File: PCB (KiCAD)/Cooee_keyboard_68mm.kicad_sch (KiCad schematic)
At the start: 99 parts, among them J1 Conn_01x15_Pin

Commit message: finished routing new smaller keyboard
finished routing new smaller keyboard
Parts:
- removed H1: MountingHole, MountingHole:MountingHole_3.2mm_M3_ISO7380_Pad, symbol Mechanical:MountingHole
- H4, H5: footprint MountingHole:MountingHole_3.2mm_M3_ISO7380_Pad -> MountingHole:MountingHole_3.2mm_M3
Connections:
- net COL1: now also D5.1 (K); no longer D7.1 (K)
- net COL2: now also D51.1 (K), D7.1 (K); no longer D14.1 (K), D5.1 (K)
- net COL3: now also D14.1 (K); no longer D17.1 (K)
- net COL4: now also D17.1 (K); no longer D21.1 (K)
- net COL5: now also D21.1 (K); no longer D22.1 (K), D92.1 (K)
- net COL6: now also D22.1 (K), D92.1 (K); no longer D27.1 (K), D93.1 (K)
- net COL7: now also D27.1 (K), D93.1 (K), J1.4 (Pin_4); no longer D28.2 (A), D31.1 (K), J1.9 (Pin_9)
- net COL8: now also D28.2 (A), D31.1 (K), J1.3 (Pin_3); no longer D51.1 (K), D52.1 (K), D54.1 (K), J1.8 (Pin_8)
- net COL9: now also D52.1 (K), J1.2 (Pin_2); no longer D39.1 (K), D44.1 (K), J1.7 (Pin_7)
- net ROW1: now also J1.9 (Pin_9), SWe29.1; no longer J1.6 (Pin_6)
- net ROW2: now also J1.8 (Pin_8), SWe36.1, SWe37.1; no longer J1.5 (Pin_5), SWe29.1
- net ROW3: now also J1.7 (Pin_7), SWe39.1; no longer J1.4 (Pin_4), SWe36.1
- net ROW4: now also J1.6 (Pin_6), SWe17.1, SWe24.1; no longer J1.3 (Pin_3), SWe39.1, SWe47.1
- net ROW5: now also J1.5 (Pin_5), SWe2.1, SWe47.1, SWe50.1; no longer J1.2 (Pin_2), SWe17.1, SWe24.1
- removed net ROW6: J1.1 (Pin_1), SWe2.1, SWe37.1, SWe50.1
- new net COL10: D39.1 (K), D44.1 (K), D54.1 (K), J1.1 (Pin_1)
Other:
- moved on the sheet: D14, D17, D21, D22, D27, D28, D3, D31, D32, D39, D43, D44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

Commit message: finished keyboard at 67mm
started work on esp32 motherboard
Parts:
- removed H4, H5, H7: MountingHole, MountingHole:MountingHole_3.2mm_M3, symbol Mechanical:MountingHole
- removed J1: Conn_01x15_Pin, Connector_PinHeader_2.54mm:PinHeader_1x15_P2.54mm_Vertical, symbol Connector:Conn_01x15_Pin
- added D4, D40, D47, D6: SS24, Diode_SMD:D_0805_2012Metric, symbol Diode:SS24
- added J1: Conn_02x20_Counter_Clockwise, Connector_PinHeader_2.54mm:PinHeader_2x20_P2.54mm_Vertical_SMD, symbol Connector_Generic:Conn_02x20_Counter_Clockwise
- added J2, J3, J4, J5, J6, J7: Conn_01x01_Pin, USB4105-GF-A (1):Lil_Pad, symbol Connector:Conn_01x01_Pin
- added R2, R3, R4, R6: R, Resistor_SMD:R_0805_2012Metric_Pad1.20x1.40mm_HandSolder, symbol Device:R
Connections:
- net COL1: now also J1.1 (Pin_1), J1.2 (Pin_2)
- net COL10: now also J1.39 (Pin_39), J1.40 (Pin_40)
- net COL2: now also J1.5 (Pin_5), J1.6 (Pin_6)
- net COL3: now also J1.10 (Pin_10), J1.9 (Pin_9)
- net COL4: now also J1.15 (Pin_15), J1.16 (Pin_16)
- net COL5: now also J1.19 (Pin_19), J1.20 (Pin_20)
- net COL6: now also J1.27 (Pin_27), J1.28 (Pin_28)
- net COL7: now also J1.33 (Pin_33), J1.34 (Pin_34)
- net COL8: now also J1.35 (Pin_35), J1.36 (Pin_36)
- net COL9: now also J1.37 (Pin_37), J1.38 (Pin_38)
- net ROW1: now also J1.3 (Pin_3), J1.4 (Pin_4)
- net ROW2: now also J1.7 (Pin_7), J1.8 (Pin_8)
- net ROW3: now also J1.11 (Pin_11), J1.12 (Pin_12)
- net ROW4: now also J1.13 (Pin_13), J1.14 (Pin_14)
- net ROW5: now also J1.17 (Pin_17), J1.18 (Pin_18)
- new net: D4.1 (K), R2.1
- new net: D40.1 (K), R4.1
- new net: D6.1 (K), R3.1
- new net: D47.1 (K), R6.1
- new net +3.3V: D4.2 (A), D40.2 (A), D47.2 (A), D6.2 (A), J1.31 (Pin_31), J1.32 (Pin_32)
- new net GND: J1.29 (Pin_29), J1.30 (Pin_30), R2.2, R3.2, R4.2, R6.2
- new net SPARE1: J1.26 (Pin_26), J2.1 (Pin_1)
- new net SPARE2: J1.25 (Pin_25), J3.1 (Pin_1)
- new net SPARE3: J1.24 (Pin_24), J4.1 (Pin_1)
- new net SPARE4: J1.23 (Pin_23), J5.1 (Pin_1)
- new net SPARE5: J1.22 (Pin_22), J6.1 (Pin_1)
- new net SPARE6: J1.21 (Pin_21), J7.1 (Pin_1)
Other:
- moved on the sheet: D10, D11, D12, D13, D14, D15, D16, D17, D18, D19, D2, D20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

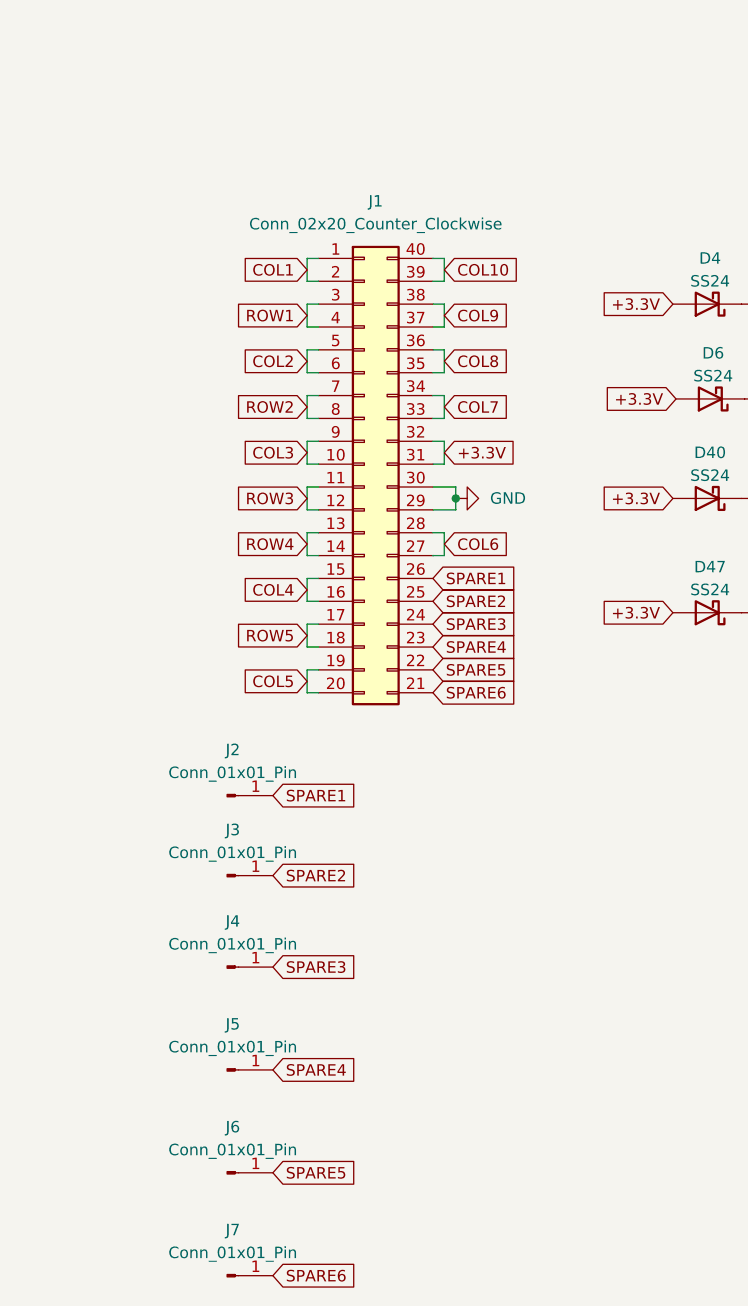
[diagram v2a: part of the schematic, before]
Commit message: more PCB work
should have the 90 degree SMD header pins lined up to mount now, unfortunately I've invalidated the keyboard prototypes I already bought
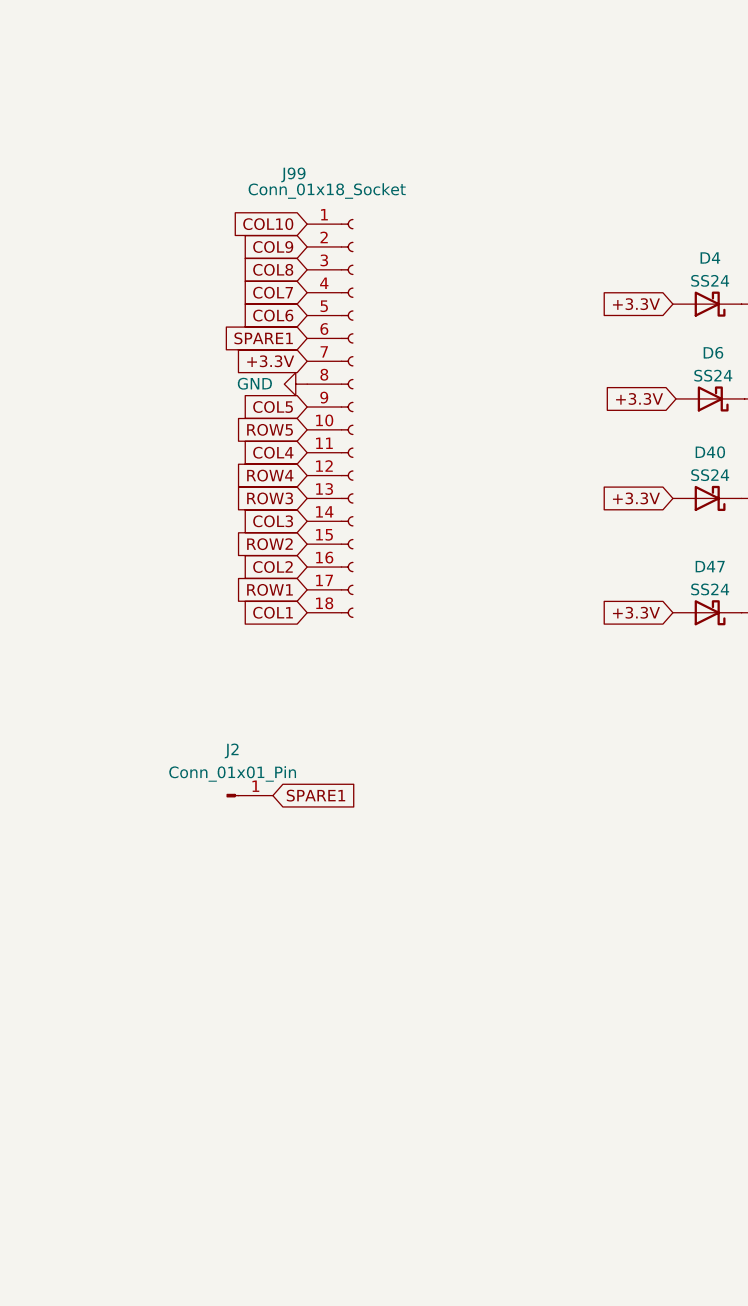
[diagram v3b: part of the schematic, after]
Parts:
- removed J1: Conn_02x20_Counter_Clockwise, Connector_PinHeader_2.54mm:PinHeader_2x20_P2.54mm_Vertical_SMD, symbol Connector_Generic:Conn_02x20_Counter_Clockwise
- removed J3, J4, J5, J6, J7: Conn_01x01_Pin, USB4105-GF-A (1):Lil_Pad, symbol Connector:Conn_01x01_Pin
- added J99: Conn_01x18_Socket, USB4105-GF-A (1):SMD_Header_1x18_P2.54mm, symbol Connector:Conn_01x18_Socket
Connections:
- net +3.3V: now also J99.7 (Pin_7)
- net COL1: now also J99.18 (Pin_18)
- net COL10: now also J99.1 (Pin_1)
- net COL2: now also J99.16 (Pin_16)
- net COL3: now also J99.14 (Pin_14)
- net COL4: now also J99.11 (Pin_11)
- net COL5: now also J99.9 (Pin_9)
- net COL6: now also J99.5 (Pin_5)
- net COL7: now also J99.4 (Pin_4)
- net COL8: now also J99.3 (Pin_3)
- net COL9: now also J99.2 (Pin_2)
- net GND: now also J99.8 (Pin_8)
- net ROW1: now also J99.17 (Pin_17)
- net ROW2: now also J99.15 (Pin_15)
- net ROW3: now also J99.13 (Pin_13)
- net ROW4: now also J99.12 (Pin_12)
- net ROW5: now also J99.10 (Pin_10)
- net SPARE1: now also J99.6 (Pin_6)

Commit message: new IC choices for GPS, audio and power
also added a keyboard IC to the keyboard to preventing wasting precious ESP32 GPIOs
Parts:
- removed J2: Conn_01x01_Pin, USB4105-GF-A (1):Lil_Pad, symbol Connector:Conn_01x01_Pin
- removed J99: Conn_01x18_Socket, USB4105-GF-A (1):SMD_Header_1x18_P2.54mm, symbol Connector:Conn_01x18_Socket
- added R1, R5, R7: 10k, Resistor_SMD:R_0805_2012Metric_Pad1.20x1.40mm_HandSolder, symbol Device:R
- added U1: TCA8418RTWR, USB4105-GF-A (1):QFN50P400X400X100-25N, symbol Downloaded:TCA8418RTWR
- R2, R3, R4, R6: value R -> 1000
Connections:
- net +3.3V: now also R1.2, R5.2, R7.1, U1.21 (VCC)
- net COL1: now also U1.9 (COL0)
- net COL10: now also U1.18 (COL9)
- net COL2: now also U1.10 (COL1)
- net COL3: now also U1.11 (COL2)
- net COL4: now also U1.12 (COL3)
- net COL5: now also U1.13 (COL4)
- net COL6: now also U1.14 (COL5)
- net COL7: now also U1.15 (COL6)
- net COL8: now also U1.16 (COL7)
- net COL9: now also U1.17 (COL8)
- net GND: now also U1.19 (GND)
- net ROW1: now also U1.8 (ROW0)
- net ROW2: now also U1.7 (ROW1)
- net ROW3: now also U1.6 (ROW2)
- net ROW4: now also U1.5 (ROW3)
- net ROW5: now also U1.4 (ROW4)
- net SPARE1: now also U1.24 (~{INT})
- new net: R7.2, U1.25 (EP)
- new net KEEB_D: R5.1, U1.22 (SDA)
- new net KEEB_SCL: R1.1, U1.23 (SCL)
- new net KEEP_RST: U1.20 (~{RESET})

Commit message: finalized next prototype of keyboard PCB, ready to order
finalized next prototype of keyboard PCB, ready to order
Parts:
- added H1, H2: MountingHole_Pad, MountingHole:MountingHole_3.2mm_M3_DIN965_Pad_TopBottom, symbol Mechanical:MountingHole_Pad
- added J9: Conn_01x05_Pin, Connector_PinHeader_2.54mm:PinHeader_1x05_P2.54mm_Horizontal, symbol Connector:Conn_01x05_Socket
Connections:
- net +3.3V: now also R7.2, J9.2 (Pin_2); no longer R7.1
- net COL1: now also D39.1 (K), D44.1 (K), D54.1 (K), U1.12 (COL3); no longer D2.1 (K), D3.1 (K), D5.1 (K), D8.1 (K), D9.1 (K), U1.9 (COL0)
- net COL10: now also D2.1 (K), D3.1 (K), D5.1 (K), D8.1 (K), D9.1 (K); no longer D39.1 (K), D44.1 (K), D54.1 (K)
- net COL2: now also D32.1 (K), D38.1 (K), D43.1 (K), D46.1 (K), D52.1 (K), U1.11 (COL2); no longer D10.1 (K), D12.1 (K), D13.1 (K), D51.1 (K), D7.1 (K), U1.10 (COL1)
- net COL3: now also D28.2 (A), D31.1 (K), D37.1 (K), D42.1 (K), D45.1 (K), U1.10 (COL1); no longer D11.1 (K), D14.1 (K), D15.1 (K), D16.1 (K), U1.11 (COL2)
- net COL4: now also D27.1 (K), D29.1 (K), D30.1 (K), D36.1 (K), D93.1 (K), U1.9 (COL0); no longer D17.1 (K), D19.1 (K), D20.1 (K), D33.1 (K), D91.1 (K), U1.12 (COL3)
- net COL7: now also D17.1 (K), D19.1 (K), D20.1 (K), D33.1 (K), D91.1 (K); no longer D27.1 (K), D29.1 (K), D30.1 (K), D36.1 (K), D93.1 (K)
- net COL8: now also D11.1 (K), D14.1 (K), D15.1 (K), D16.1 (K); no longer D28.2 (A), D31.1 (K), D37.1 (K), D42.1 (K), D45.1 (K)
- net COL9: now also D10.1 (K), D12.1 (K), D13.1 (K), D51.1 (K), D7.1 (K); no longer D32.1 (K), D38.1 (K), D43.1 (K), D46.1 (K), D52.1 (K)
- net GND: now also H1.1, H2.1, J9.1 (Pin_1)
- net KEEB_D: now also J9.3 (Pin_3)
- net KEEB_SCL: now also J9.4 (Pin_4)
- net at U1.25 (EP): no longer R7.2
- net KEEP_RST renamed KEEB_RST
- net KEEB_RST: now also R7.1
- net SPARE1 renamed KEEB_INT
- net KEEB_INT: now also J9.5 (Pin_5)
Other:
- moved on the sheet: R1, R5
